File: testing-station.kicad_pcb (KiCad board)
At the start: 2 copper layers, 212.7 x 113.3 mm, 88 parts, among them IC1 BME680, IC2 DS3231, IC3 74HC4050D, IC4 LP2985A, J1 pyranometer, J13 microSD, J2 anemometer, J3 AM2315C, J4 FPC connector, J5 Pt100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

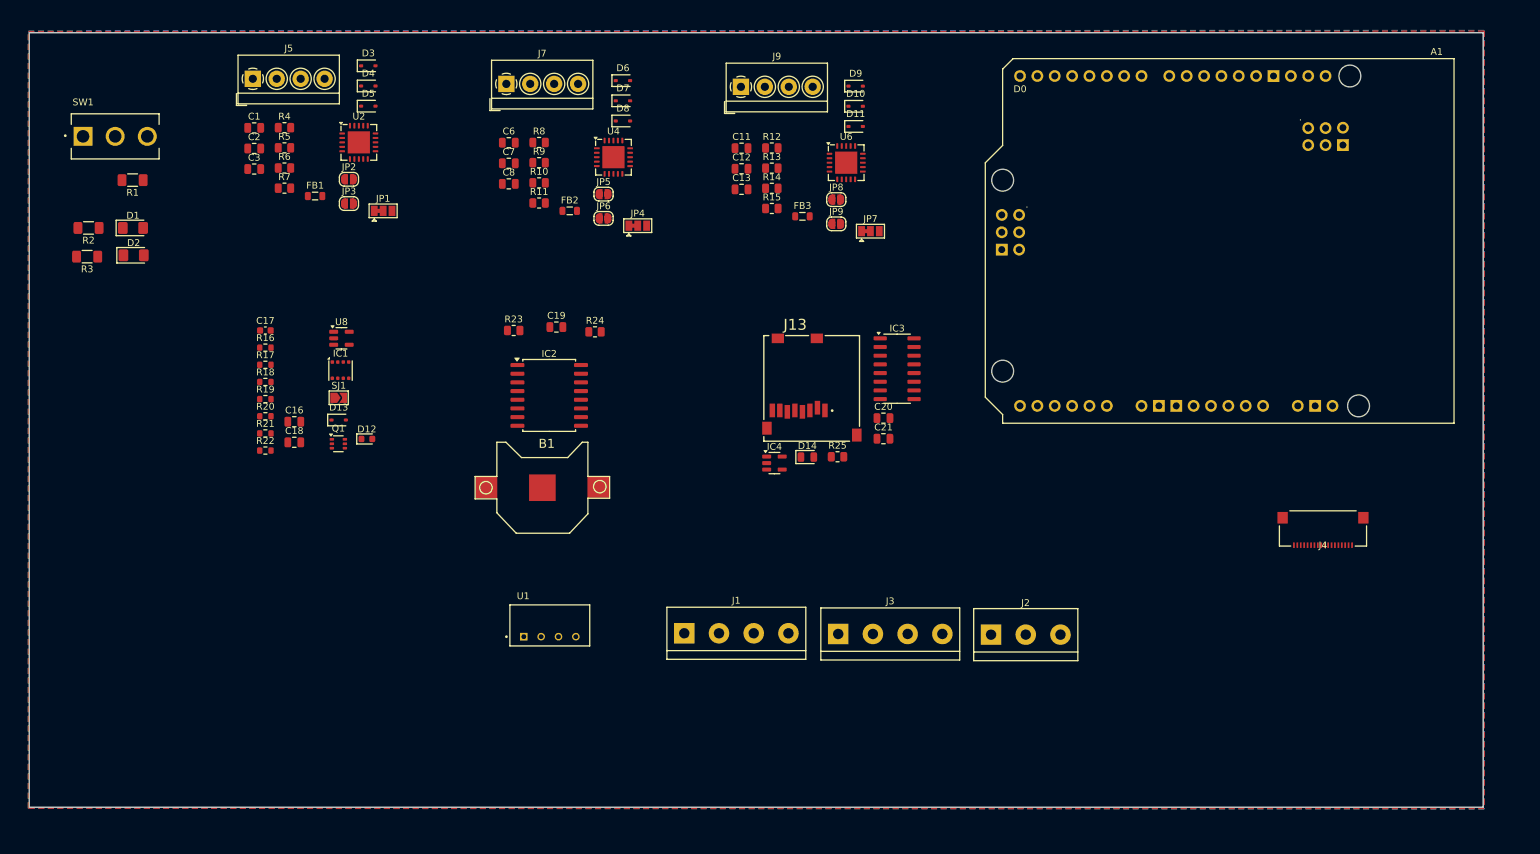
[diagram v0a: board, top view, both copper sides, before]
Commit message: MAX31865 routed on PCB
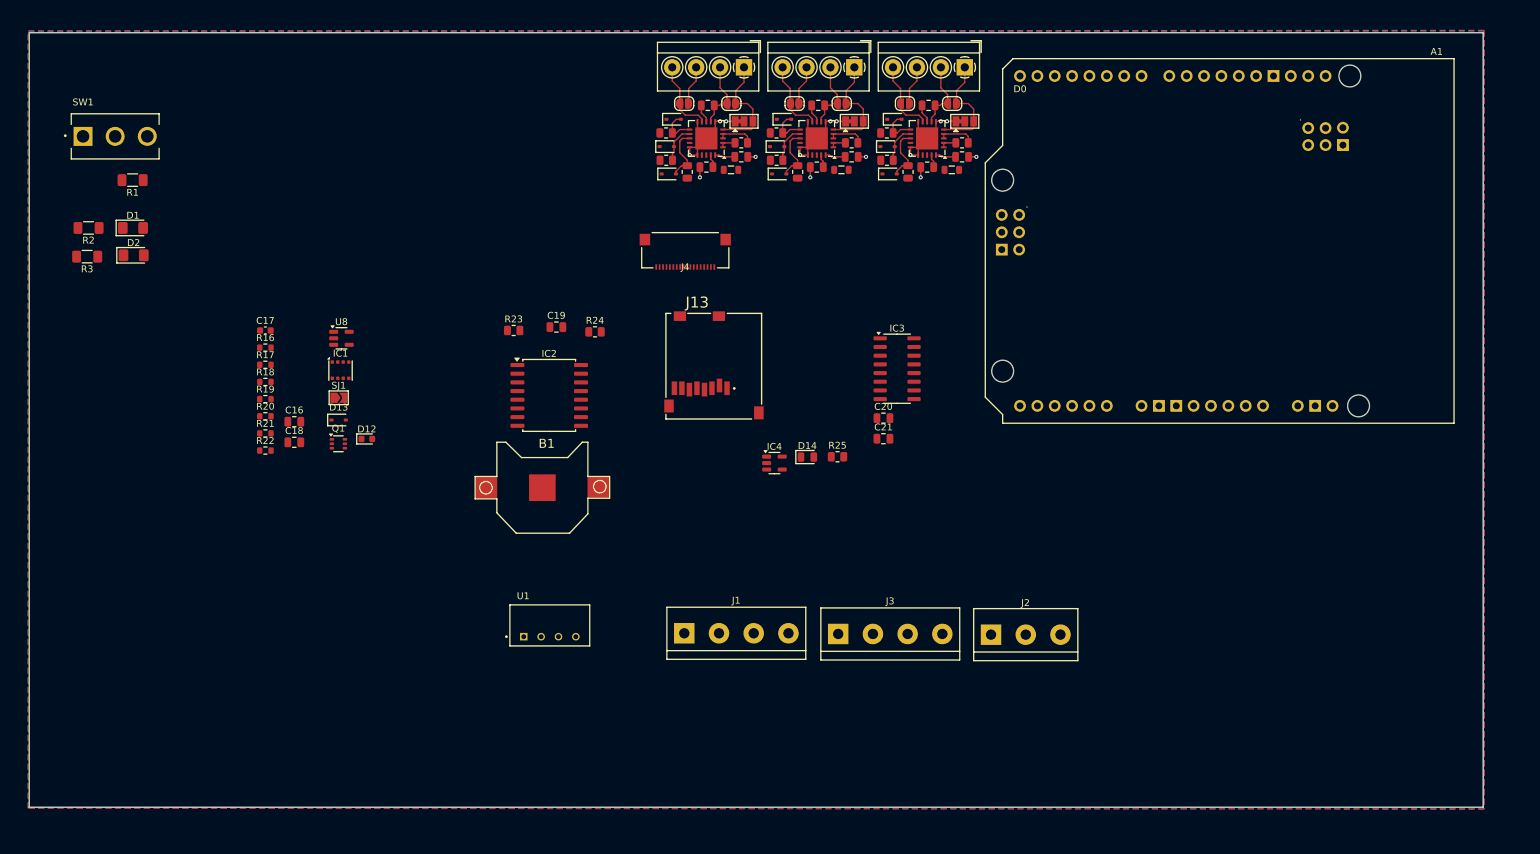
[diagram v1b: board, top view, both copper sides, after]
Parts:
- removed the R10 at (116.2, 43.5)
- removed R14: 10K, Resistor_SMD:R_0805_2012Metric
- added R10: 10K, Resistor_SMD:R_0805_2012Metric, F.Cu at (150.9, 36.2)
- added R10: 10K, Resistor_SMD:R_0805_2012Metric, F.Cu at (167.1, 36.2)
- moved J4 101.8 mm to (137.6, 53.4)
- moved J5 71.9 mm to (146.2, 26.6), turned to 180 degrees
- moved C2 71.3 mm to (145.8, 39.7)
- moved R7 67.2 mm to (145.8, 37.6), turned to 180 degrees
- moved C3 67.0 mm to (140.9, 32.2), turned to 180 degrees
- moved C1 66.4 mm to (140.7, 41.2), turned to 180 degrees
- moved FB1 61.0 mm to (144.3, 41.6)
- moved R4 59.3 mm to (137.9, 41.9), turned to -90 degrees
- moved JP2 57.0 mm to (144.3, 31.9)
- moved R6 56.1 mm to (134.8, 36.2), turned to 180 degrees
- moved R5 55.9 mm to (134.8, 40.2), turned to 180 degrees
- moved JP1 54.4 mm to (146.2, 34.5)
- moved JP3 51.2 mm to (137.4, 31.9)
- moved J7 51.0 mm to (162.3, 26.6), turned to 180 degrees
- moved U2 50.8 mm to (140.7, 37.0), turned to 180 degrees
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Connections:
- C12 pad 1: Net-(U6-VDD) -> Net-(U4-VDD)
- C13 pad 1: Net-(J9-Pin_2) -> Net-(J7-Pin_2)
- C13 pad 2: Net-(J9-Pin_3) -> Net-(J7-Pin_3)
- D10 pad 2: Net-(D10-A) -> Net-(D7-A)
- D11 pad 1: /A3 -> /A2
- D11 pad 2: Net-(D11-A) -> Net-(D8-A)
- D9 pad 2: Net-(D9-A) -> Net-(D6-A)
- FB3 pad 1: Net-(U6-VDD) -> Net-(U4-VDD)
- J9 pad 1: Net-(J9-Pin_1) -> Net-(J7-Pin_1)
- J9 pad 2: Net-(J9-Pin_2) -> Net-(J7-Pin_2)
- J9 pad 3: Net-(J9-Pin_3) -> Net-(J7-Pin_3)
- J9 pad 4: Net-(J9-Pin_4) -> Net-(J7-Pin_4)
- JP7 pad 3: Net-(J9-Pin_1) -> Net-(J7-Pin_1)
- JP8 pad 1: Net-(J9-Pin_2) -> Net-(J7-Pin_2)
- JP8 pad 2: Net-(J9-Pin_1) -> Net-(J7-Pin_1)
- JP9 pad 1: Net-(J9-Pin_4) -> Net-(J7-Pin_4)
- JP9 pad 2: Net-(J9-Pin_3) -> Net-(J7-Pin_3)
- R12 pad 1: Net-(D11-A) -> Net-(D8-A)
- R13 pad 1: Net-(D10-A) -> Net-(D7-A)
- R15 pad 1: Net-(U6-ISENSOR) -> Net-(U4-ISENSOR)
- R15 pad 2: Net-(U6-BIAS) -> Net-(U4-BIAS)
- U2 pad 18: /MAX31865_1/DRDY -> unconnected-(U2-~{DRDY}-Pad18)
- U4 pad 18: /MAX31865_2/DRDY -> unconnected-(U4-~{DRDY}-Pad18)
- U6 pad 1: Net-(U6-BIAS) -> Net-(U4-BIAS)
- U6 pad 11: Net-(D9-A) -> Net-(D6-A)
- U6 pad 12: Net-(D10-A) -> Net-(D7-A)
- U6 pad 13: Net-(D11-A) -> Net-(D8-A)
- U6 pad 17: unconnected-(U6-NC-Pad17) -> unconnected-(U4-NC-Pad17)
- U6 pad 18: /MAX31865_3/DRDY -> unconnected-(U4-~{DRDY}-Pad18)
- U6 pad 2: Net-(U6-BIAS) -> Net-(U4-BIAS)
- U6 pad 20: Net-(U6-VDD) -> Net-(U4-VDD)
- U6 pad 3: Net-(U6-ISENSOR) -> Net-(U4-ISENSOR)
- U6 pad 4: Net-(U6-ISENSOR) -> Net-(U4-ISENSOR)
- U6 pad 5: Net-(J9-Pin_1) -> Net-(J7-Pin_1)
- U6 pad 7: Net-(J9-Pin_2) -> Net-(J7-Pin_2)
- U6 pad 8: Net-(J9-Pin_3) -> Net-(J7-Pin_3)
- U6 pad 9: Net-(J9-Pin_4) -> Net-(J7-Pin_4)
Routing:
- net GND: track 0.00 -> 51.3 mm, vias 0 -> 15
- net Net-(J7-Pin_1): track 0.00 -> 31.7 mm
- net Net-(J7-Pin_4): track 0.00 -> 21.7 mm
- net Net-(J7-Pin_2): track 0.00 -> 20.1 mm
- net Net-(J7-Pin_3): track 0.00 -> 16.4 mm
- net Net-(D8-A): track 0.00 -> 16.1 mm
- net Net-(J5-Pin_1): track 0.00 -> 15.9 mm
- net Net-(D6-A): track 0.00 -> 11.3 mm
- net Net-(D7-A): track 0.00 -> 11.1 mm
- net Net-(J5-Pin_4): track 0.00 -> 10.9 mm
- net Net-(U4-ISENSOR): track 0.00 -> 10.6 mm
- net Net-(J5-Pin_2): track 0.00 -> 10.0 mm
- net Net-(J5-Pin_3): track 0.00 -> 8.22 mm
- net Net-(D5-A): track 0.00 -> 8.05 mm
- net Net-(U4-VDD): track 0.00 -> 5.94 mm
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
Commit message: DS3231 routed on PCB
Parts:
- removed C16, C18, C20: 10uF, Capacitor_SMD:C_0805_2012Metric
- removed C17: 0.1uF, Capacitor_SMD:C_0603_1608Metric
- removed C19: 1uF, Capacitor_SMD:C_0805_2012Metric
- removed C21: 0.1uF, Capacitor_SMD:C_0805_2012Metric
- removed IC4: LP2985A, Package_TO_SOT_SMD:SOT-23-5
- removed U8: AP2112K-3.3, Package_TO_SOT_SMD:SOT-23-5
- moved B1 127.6 mm to (240.8, 58.3), turned to -90 degrees
- moved IC2 116.4 mm to (230.2, 44.7), turned to 180 degrees
- moved R23 111.1 mm to (222.6, 49.9)
- moved R24 99.7 mm to (222.6, 47.9)
- moved A1 13.2 mm to (260.6, 86.7)
- moved IC3 11.8 mm to (156.9, 69.4)
- renumbered R10 to R14
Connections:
- A1 pad 3V3: unconnected-(A1-3.3V-Pad3V3) -> +3.3V
- A1 pad GND1: unconnected-(A1-GND-PadGND1) -> GND
- A1 pad GND2: unconnected-(A1-GND-PadGND2) -> GND
- A1 pad GND3: unconnected-(A1-GND-PadGND3) -> GND
- A1 pad GND4: unconnected-(A1-GND-PadGND4)_0 -> GND
- A1 pad GND5: unconnected-(A1-GND-PadGND5) -> GND
- C12 pad 1: Net-(U4-VDD) -> Net-(U6-VDD)
- C13 pad 1: Net-(J7-Pin_2) -> Net-(J9-Pin_2)
- C13 pad 2: Net-(J7-Pin_3) -> Net-(J9-Pin_3)
- D10 pad 2: Net-(D7-A) -> Net-(D10-A)
- D11 pad 1: /A2 -> /A3
- D11 pad 2: Net-(D8-A) -> Net-(D11-A)
- D9 pad 2: Net-(D6-A) -> Net-(D9-A)
- FB3 pad 1: Net-(U4-VDD) -> Net-(U6-VDD)
- IC2 pad 1: /DS3231/32KHZ -> unconnected-(IC2-32KHZ-Pad1)
- IC2 pad 3: /DS3231/SQW -> unconnected-(IC2-SQW/INT-Pad3)
- IC2 pad 4: /DS3231/~{RTC_RST} -> unconnected-(IC2-/RST-Pad4)
- J9 pad 1: Net-(J7-Pin_1) -> Net-(J9-Pin_1)
- J9 pad 2: Net-(J7-Pin_2) -> Net-(J9-Pin_2)
- J9 pad 3: Net-(J7-Pin_3) -> Net-(J9-Pin_3)
- J9 pad 4: Net-(J7-Pin_4) -> Net-(J9-Pin_4)
- JP7 pad 3: Net-(J7-Pin_1) -> Net-(J9-Pin_1)
- JP8 pad 1: Net-(J7-Pin_2) -> Net-(J9-Pin_2)
- JP8 pad 2: Net-(J7-Pin_1) -> Net-(J9-Pin_1)
- JP9 pad 1: Net-(J7-Pin_4) -> Net-(J9-Pin_4)
- JP9 pad 2: Net-(J7-Pin_3) -> Net-(J9-Pin_3)
- R12 pad 1: Net-(D8-A) -> Net-(D11-A)
- R13 pad 1: Net-(D7-A) -> Net-(D10-A)
- R14 pad 1: Net-(D6-A) -> Net-(D9-A)
- R15 pad 1: Net-(U4-ISENSOR) -> Net-(U6-ISENSOR)
- R15 pad 2: Net-(U4-BIAS) -> Net-(U6-BIAS)
- U6 pad 1: Net-(U4-BIAS) -> Net-(U6-BIAS)
- U6 pad 11: Net-(D6-A) -> Net-(D9-A)
- U6 pad 12: Net-(D7-A) -> Net-(D10-A)
- U6 pad 13: Net-(D8-A) -> Net-(D11-A)
- U6 pad 17: unconnected-(U4-NC-Pad17) -> unconnected-(U6-NC-Pad17)
- U6 pad 18: unconnected-(U4-~{DRDY}-Pad18) -> unconnected-(U6-~{DRDY}-Pad18)
- U6 pad 2: Net-(U4-BIAS) -> Net-(U6-BIAS)
- U6 pad 20: Net-(U4-VDD) -> Net-(U6-VDD)
- U6 pad 3: Net-(U4-ISENSOR) -> Net-(U6-ISENSOR)
- U6 pad 4: Net-(U4-ISENSOR) -> Net-(U6-ISENSOR)
- U6 pad 5: Net-(J7-Pin_1) -> Net-(J9-Pin_1)
- U6 pad 7: Net-(J7-Pin_2) -> Net-(J9-Pin_2)
- U6 pad 8: Net-(J7-Pin_3) -> Net-(J9-Pin_3)
- U6 pad 9: Net-(J7-Pin_4) -> Net-(J9-Pin_4)
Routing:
- net /SCL: track 0.00 -> 26.6 mm, vias 0 -> 1
- net /SCA: track 0.00 -> 22.5 mm, vias 0 -> 1
- net /DS3231/VBAT: track 0.00 -> 16.6 mm
- net Net-(J9-Pin_1): track 0.00 -> 15.9 mm
- net Net-(J7-Pin_1): track 31.7 -> 15.9 mm
- net Net-(J9-Pin_4): track 0.00 -> 10.9 mm
- net Net-(J7-Pin_4): track 21.7 -> 10.9 mm
- net Net-(J9-Pin_2): track 0.00 -> 10.0 mm
- net Net-(J7-Pin_2): track 20.1 -> 10.0 mm
- net Net-(J9-Pin_3): track 0.00 -> 8.22 mm
- net Net-(J7-Pin_3): track 16.4 -> 8.22 mm
- net Net-(D8-A): track 16.1 -> 8.05 mm
- net Net-(D11-A): track 0.00 -> 8.05 mm
- net Net-(D9-A): track 0.00 -> 5.64 mm
- net Net-(D6-A): track 11.3 -> 5.64 mm
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
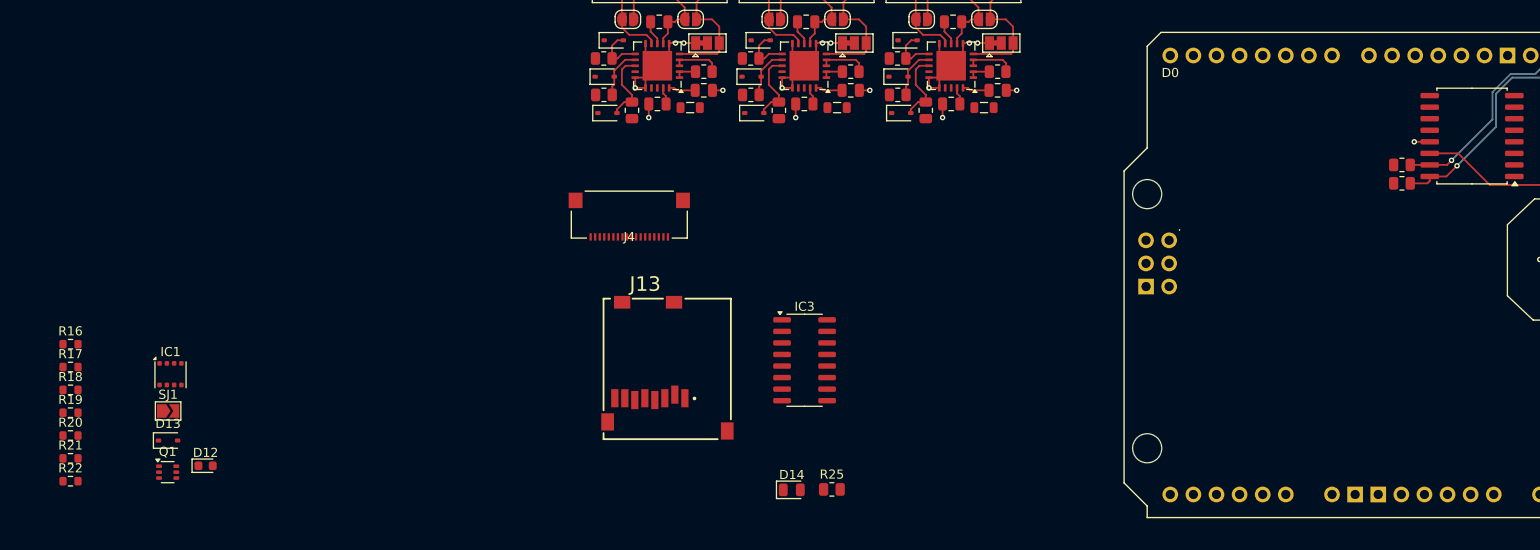
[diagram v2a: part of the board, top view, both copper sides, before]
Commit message: BME680 routed on PCB
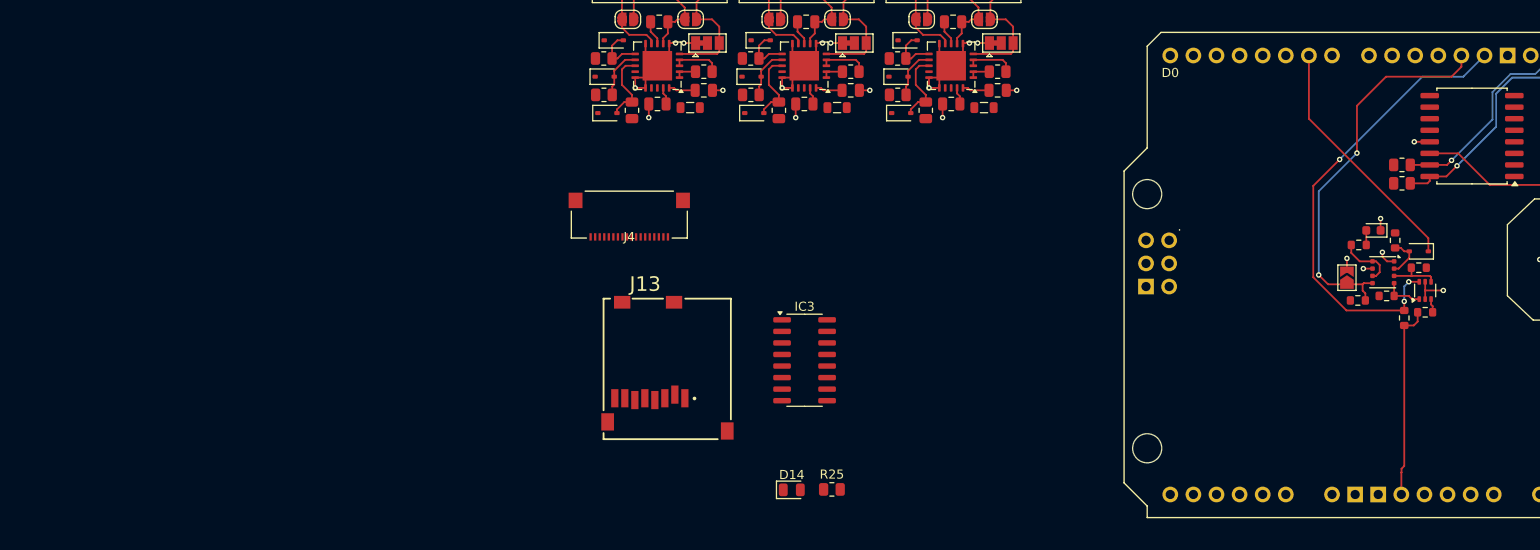
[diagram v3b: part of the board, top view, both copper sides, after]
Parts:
- moved R20 149.4 mm to (224.4, 59.2), turned to 180 degrees
- moved R18 149.2 mm to (225.1, 64.1)
- moved R21 147.6 mm to (221.8, 56.2), turned to 90 degrees
- moved R17 146.7 mm to (222.8, 64.7), turned to 90 degrees
- moved R19 145.3 mm to (220.9, 62.3)
- moved R22 142.9 mm to (217.7, 62.8), turned to 180 degrees
- moved R16 142.0 mm to (217.8, 56.7)
- moved Q1 139.7 mm to (225.1, 61.7), turned to 90 degrees
- moved D13 139.1 mm to (224.4, 57.4), turned to 180 degrees
- moved IC1 133.8 mm to (220.5, 59.7), turned to -90 degrees
- moved D12 131.0 mm to (219.4, 55.1), turned to 180 degrees
- moved SJ1 130.4 mm to (216.5, 60.3), turned to 90 degrees
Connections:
- A1 pad 5V1: unconnected-(A1-5V-Pad5V1) -> +5V
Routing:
- net /SCK: track 0.00 -> 50.9 mm, vias 0 -> 3
- net /MISO: track 0.00 -> 44.0 mm, vias 0 -> 2
- net /D6: track 0.00 -> 27.0 mm
- net +5V: track 0.00 -> 21.4 mm
- net +3.3V: track 5.67 -> 15.9 mm, vias 0 -> 1
- net GND: track 56.1 -> 61.8 mm, vias 17 -> 21
- net /BME680/SDI_3V: track 0.00 -> 5.53 mm
- net /BME680/CS_3V: track 0.00 -> 4.58 mm
- net /BME680/SCK_3V: track 0.00 -> 4.31 mm
- net Net-(D12-A): track 0.00 -> 1.60 mm
- net /MOSI: track 0.00 -> 1.52 mm
